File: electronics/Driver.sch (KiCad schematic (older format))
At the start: 27 parts

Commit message: Attached footprints to components
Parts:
- C10, C13, C16: renamed from C?; footprint (none) -> Capacitor_THT:CP_Radial_D8.0mm_P3.50mm
- C12, C15, C18: renamed from C?; footprint Resistor_SMD:R_0603_1608Metric_Pad0.98x0.95mm_HandSolder -> Capacitor_SMD:C_0603_1608Metric_Pad1.08x0.95mm_HandSolder
- J1, J2, J3, J4, J5, J6: renamed from J?; footprint (none) -> Electronics:3mm_pad
- R10, R11, R12, R13, R5, R6, R7, R8, R9: renamed from R?; footprint (none) -> Resistor_SMD:R_0603_1608Metric_Pad0.98x0.95mm_HandSolder
- gave numbers to parts that had none: 6

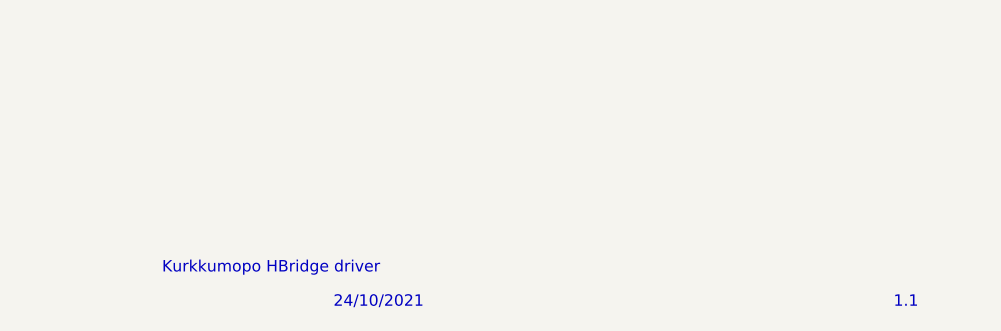
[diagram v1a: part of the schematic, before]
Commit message: Figured out how to automatically change date and revision
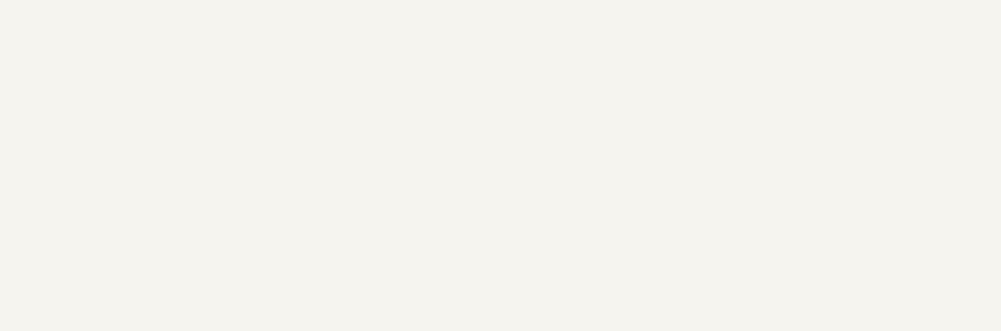
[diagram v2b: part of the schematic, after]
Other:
- note removed: "1.1"
- note removed: "24/10/2021"
- note removed: "Kurkkumopo HBridge driver"
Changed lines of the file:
@@
 encoding utf-8
 Sheet 2 3
-Title ""
-Date ""
-Rev ""
+Title "Kurkkumopo HBridge driver"
+Date "2021-11-01"
+Rev "1.2"
 Comp ""
 Comment1 ""
@@
 EndData
 $EndBitmap
-Text Notes 7350 7500 0    50   ~ 0
-Kurkkumopo HBridge driver
-Text Notes 8100 7650 0    50   ~ 0
-24/10/2021
-Text Notes 10550 7650 0    50   ~ 0
-1.1
 $Comp
 L Device:R R?

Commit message: Relocated items
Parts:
- C10, C13, C16: value 47uF -> 100uF; footprint Capacitor_THT:CP_Radial_D8.0mm_P3.50mm -> Capacitor_SMD:CP_Elec_8x10
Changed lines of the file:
@@
 Wire Wire Line
 	2750 2400 2850 2400
-$Comp
-L Device:CP C10
-U 1 1 6160C840
-P 2600 1100
-F 0 "C10" V 2855 1100 50  0000 C CNN
-F 1 "47uF" V 2764 1100 50  0000 C CNN
-F 2 "Capacitor_THT:CP_Radial_D8.0mm_P3.50mm" H 2638 950 50  0001 C CNN
-F 3 "~" H 2600 1100 50  0001 C CNN
-	1    2600 1100
-	0    -1   -1   0
-$EndComp
 Wire Wire Line
 	2300 1050 2300 1100
@@
 Wire Wire Line
 	6400 2400 6500 2400
-$Comp
-L Device:CP C13
-U 1 1 6160C8B7
-P 6250 1100
-F 0 "C13" V 6505 1100 50  0000 C CNN
-F 1 "47uF" V 6414 1100 50  0000 C CNN
-F 2 "Capacitor_THT:CP_Radial_D8.0mm_P3.50mm" H 6288 950 50  0001 C CNN
-F 3 "~" H 6250 1100 50  0001 C CNN
-	1    6250 1100
-	0    -1   -1   0
-$EndComp
 Wire Wire Line
 	5950 1050 5950 1100
@@
 Wire Wire Line
 	9850 2400 9950 2400
-$Comp
-L Device:CP C16
-U 1 1 6160C92E
-P 9700 1100
-F 0 "C16" V 9955 1100 50  0000 C CNN
-F 1 "47uF" V 9864 1100 50  0000 C CNN
-F 2 "Capacitor_THT:CP_Radial_D8.0mm_P3.50mm" H 9738 950 50  0001 C CNN
-F 3 "~" H 9700 1100 50  0001 C CNN
-	1    9700 1100
-	0    -1   -1   0
-$EndComp
 Wire Wire Line
 	9400 1050 9400 1100
@@
 	-1   0    0    1
 $EndComp
+$Comp
+L Device:CP C?
+U 1 1 6189E08C
+P 2600 1100
+AR Path="/615F51F3/6189E08C" Ref="C?"  Part="1"
+AR Path="/617B7795/6189E08C" Ref="C?"  Part="1"
+AR Path="/615F228F/6189E08C" Ref="C10"  Part="1"
+F 0 "C10" V 2345 1100 50  0000 C CNN
+F 1 "100uF" V 2436 1100 50  0000 C CNN
+F 2 "Capacitor_SMD:CP_Elec_8x10" H 2638 950 50  0001 C CNN
+F 3 "~" H 2600 1100 50  0001 C CNN
+	1    2600 1100
+	0    1    1    0
+$EndComp
+$Comp
+L Device:CP C?
+U 1 1 6189F82C
+P 6250 1100
+AR Path="/615F51F3/6189F82C" Ref="C?"  Part="1"
+AR Path="/617B7795/6189F82C" Ref="C?"  Part="1"
+AR Path="/615F228F/6189F82C" Ref="C13"  Part="1"
+F 0 "C13" V 5995 1100 50  0000 C CNN
+F 1 "100uF" V 6086 1100 50  0000 C CNN
+F 2 "Capacitor_SMD:CP_Elec_8x10" H 6288 950 50  0001 C CNN
+F 3 "~" H 6250 1100 50  0001 C CNN
+	1    6250 1100
+	0    1    1    0
+$EndComp
+$Comp
+L Device:CP C?
+U 1 1 618A2886
+P 9700 1100
+AR Path="/615F51F3/618A2886" Ref="C?"  Part="1"
+AR Path="/617B7795/618A2886" Ref="C?"  Part="1"
+AR Path="/615F228F/618A2886" Ref="C16"  Part="1"
+F 0 "C16" V 9445 1100 50  0000 C CNN
+F 1 "100uF" V 9536 1100 50  0000 C CNN
+F 2 "Capacitor_SMD:CP_Elec_8x10" H 9738 950 50  0001 C CNN
+F 3 "~" H 9700 1100 50  0001 C CNN
+	1    9700 1100
+	0    1    1    0
+$EndComp
 $EndSCHEMATC

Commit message: Sorting componenents on pcb
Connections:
- net labels removed: GND
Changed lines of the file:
@@
 	2800 1500 2800 1600
 $Comp
-L power:GND #PWR0125
-U 1 1 6160C826
-P 2800 1600
-F 0 "#PWR0125" H 2800 1350 50  0001 C CNN
-F 1 "GND" H 2805 1427 50  0000 C CNN
-F 2 "" H 2800 1600 50  0001 C CNN
-F 3 "" H 2800 1600 50  0001 C CNN
-	1    2800 1600
-	1    0    0    -1
-$EndComp
-$Comp
 L power:Vdrive #PWR0126
 U 1 1 6160C82C
@@
 	6450 1500 6450 1600
 $Comp
-L power:GND #PWR0127
-U 1 1 6160C89D
-P 6450 1600
-F 0 "#PWR0127" H 6450 1350 50  0001 C CNN
-F 1 "GND" H 6455 1427 50  0000 C CNN
-F 2 "" H 6450 1600 50  0001 C CNN
-F 3 "" H 6450 1600 50  0001 C CNN
-	1    6450 1600
-	1    0    0    -1
-$EndComp
-$Comp
 L power:Vdrive #PWR0128
 U 1 1 6160C8A3
@@
 	9900 1500 9900 1600
 $Comp
-L power:GND #PWR0129
-U 1 1 6160C914
-P 9900 1600
-F 0 "#PWR0129" H 9900 1350 50  0001 C CNN
-F 1 "GND" H 9905 1427 50  0000 C CNN
-F 2 "" H 9900 1600 50  0001 C CNN
-F 3 "" H 9900 1600 50  0001 C CNN
-	1    9900 1600
-	1    0    0    -1
-$EndComp
-$Comp
 L power:Vdrive #PWR0130
 U 1 1 6160C91A
@@
 	0    1    1    0
 $EndComp
+$Comp
+L power:Earth #PWR?
+U 1 1 6189EC29
+P 9900 1600
+F 0 "#PWR?" H 9900 1350 50  0001 C CNN
+F 1 "Earth" H 9900 1450 50  0001 C CNN
+F 2 "" H 9900 1600 50  0001 C CNN
+F 3 "~" H 9900 1600 50  0001 C CNN
+	1    9900 1600
+	1    0    0    -1
+$EndComp
+$Comp
+L power:Earth #PWR?
+U 1 1 6189FF3E
+P 6450 1600
+F 0 "#PWR?" H 6450 1350 50  0001 C CNN
+F 1 "Earth" H 6450 1450 50  0001 C CNN
+F 2 "" H 6450 1600 50  0001 C CNN
+F 3 "~" H 6450 1600 50  0001 C CNN
+	1    6450 1600
+	1    0    0    -1
+$EndComp
+$Comp
+L power:Earth #PWR?
+U 1 1 618A18C8
+P 2800 1600
+F 0 "#PWR?" H 2800 1350 50  0001 C CNN
+F 1 "Earth" H 2800 1450 50  0001 C CNN
+F 2 "" H 2800 1600 50  0001 C CNN
+F 3 "~" H 2800 1600 50  0001 C CNN
+	1    2800 1600
+	1    0    0    -1
+$EndComp
 $EndSCHEMATC

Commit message: Allahu akbar
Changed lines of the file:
@@
 AR Path="/617B7795/6189E08C" Ref="C?"  Part="1"
 AR Path="/615F228F/6189E08C" Ref="C10"  Part="1"
-F 0 "C10" V 2345 1100 50  0000 C CNN
-F 1 "100uF" V 2436 1100 50  0000 C CNN
+F 0 "C10" V 2855 1100 50  0000 C CNN
+F 1 "100uF" V 2764 1100 50  0000 C CNN
 F 2 "Capacitor_SMD:CP_Elec_8x10" H 2638 950 50  0001 C CNN
 F 3 "~" H 2600 1100 50  0001 C CNN
 	1    2600 1100
-	0    1    1    0
+	0    -1   -1   0
 $EndComp
 $Comp
@@
 AR Path="/617B7795/6189F82C" Ref="C?"  Part="1"
 AR Path="/615F228F/6189F82C" Ref="C13"  Part="1"
-F 0 "C13" V 5995 1100 50  0000 C CNN
-F 1 "100uF" V 6086 1100 50  0000 C CNN
+F 0 "C13" V 6505 1100 50  0000 C CNN
+F 1 "100uF" V 6414 1100 50  0000 C CNN
 F 2 "Capacitor_SMD:CP_Elec_8x10" H 6288 950 50  0001 C CNN
 F 3 "~" H 6250 1100 50  0001 C CNN
 	1    6250 1100
-	0    1    1    0
+	0    -1   -1   0
 $EndComp
 $Comp
@@
 AR Path="/617B7795/618A2886" Ref="C?"  Part="1"
 AR Path="/615F228F/618A2886" Ref="C16"  Part="1"
-F 0 "C16" V 9445 1100 50  0000 C CNN
-F 1 "100uF" V 9536 1100 50  0000 C CNN
+F 0 "C16" V 9955 1100 50  0000 C CNN
+F 1 "100uF" V 9864 1100 50  0000 C CNN
 F 2 "Capacitor_SMD:CP_Elec_8x10" H 9738 950 50  0001 C CNN
 F 3 "~" H 9700 1100 50  0001 C CNN
 	1    9700 1100
-	0    1    1    0
+	0    -1   -1   0
 $EndComp
 $Comp
-L power:Earth #PWR?
+L power:Earth #PWR0125
 U 1 1 6189EC29
 P 9900 1600
-F 0 "#PWR?" H 9900 1350 50  0001 C CNN
+F 0 "#PWR0125" H 9900 1350 50  0001 C CNN
 F 1 "Earth" H 9900 1450 50  0001 C CNN
 F 2 "" H 9900 1600 50  0001 C CNN
@@
 $EndComp
 $Comp
-L power:Earth #PWR?
+L power:Earth #PWR0127
 U 1 1 6189FF3E
 P 6450 1600
-F 0 "#PWR?" H 6450 1350 50  0001 C CNN
+F 0 "#PWR0127" H 6450 1350 50  0001 C CNN
 F 1 "Earth" H 6450 1450 50  0001 C CNN
 F 2 "" H 6450 1600 50  0001 C CNN
@@
 $EndComp
 $Comp
-L power:Earth #PWR?
+L power:Earth #PWR0129
 U 1 1 618A18C8
 P 2800 1600
-F 0 "#PWR?" H 2800 1350 50  0001 C CNN
+F 0 "#PWR0129" H 2800 1350 50  0001 C CNN
 F 1 "Earth" H 2800 1450 50  0001 C CNN
 F 2 "" H 2800 1600 50  0001 C CNN
